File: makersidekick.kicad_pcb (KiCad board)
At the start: 2 copper layers, 50.8 x 22.9 mm, 30 parts, among them J2 Conn_01x12, J4 Conn_01x16

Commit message: Add hardware, almost finalize routing TODO: actually finish the pins
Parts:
- removed the REF** at (125.0, 75.5)
- removed kibuzzard-668B7879: G***, kibuzzard-668B7879
- removed kibuzzard-668B789B (x2): G***, kibuzzard-668B789B
- removed kibuzzard-668B795C: G***, kibuzzard-668B795C
- removed kibuzzard-668B797C: G***, kibuzzard-668B797C
- removed kibuzzard-668B7995: G***, kibuzzard-668B7995
- removed kibuzzard-668B79B7: G***, kibuzzard-668B79B7
- removed kibuzzard-668B79F7: G***, kibuzzard-668B79F7
- removed kibuzzard-668B7A0A: G***, kibuzzard-668B7A0A
- removed kibuzzard-668B7A1E: G***, kibuzzard-668B7A1E
- removed kibuzzard-668B7A2D: G***, kibuzzard-668B7A2D
- removed kibuzzard-668B7A62 (x2): G***, kibuzzard-668B7A62
- removed kibuzzard-668B7A7C: G***, kibuzzard-668B7A7C
- removed kibuzzard-668CCB83: G***, kibuzzard-668CCB83
- removed kibuzzard-668CCB9F: G***, kibuzzard-668CCB9F
- removed kibuzzard-668CCC45: G***, kibuzzard-668CCC45
- removed kibuzzard-668CCC52: G***, kibuzzard-668CCC52
- removed kibuzzard-668CCD74: G***, kibuzzard-668CCD74
- removed kibuzzard-668CCD89: G***, kibuzzard-668CCD89
- removed kibuzzard-668CCD9D: G***, kibuzzard-668CCD9D
- removed kibuzzard-668CCDA5: G***, kibuzzard-668CCDA5
- removed kibuzzard-668CCDB1: G***, kibuzzard-668CCDB1
- removed kibuzzard-668CE341: G***, kibuzzard-668CE341
- removed kibuzzard-668CE34C: G***, kibuzzard-668CE34C
- added ?: , , F.Cu at (180.3, 87.4)
- added Display 128x64 0.96" I2C: Display_128x64, TG9541:Display_128x64_096_I2C, F.Cu at (200.4, 93.0)
- added Display 128x64 0.96" I2C: Display_128x64, TG9541:Display_128x64_096_I2C, F.Cu at (197.0, 93.0)
- added REF**: module_mpu6050, usini_sensors:module_mpu6050, F.Cu at (173.0, 99.5)
- added REF**: R_Axial_DIN0204_L3.6mm_D1.6mm_P7.62mm_Horizontal, Resistor_THT:R_Axial_DIN0204_L3.6mm_D1.6mm_P7.62mm_Horizontal, F.Cu at (188.0, 85.3)
- moved REF** 1.06 mm to (182.5, 95.9)
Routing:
- net (no net): track 0.00 -> 225.3 mm
- net unconnected-(J2-Pin_8-Pad8): track 0.00 -> 9.30 mm
- net /GPIO_9: track 0.00 -> 2.07 mm
- net /SCL: track 0.75 -> 0.00 mm
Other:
- board size 50.8 x 22.9 mm -> 58.9 x 22.9 mm
- board text removed: "BOOT"
- board text removed: "RESET"

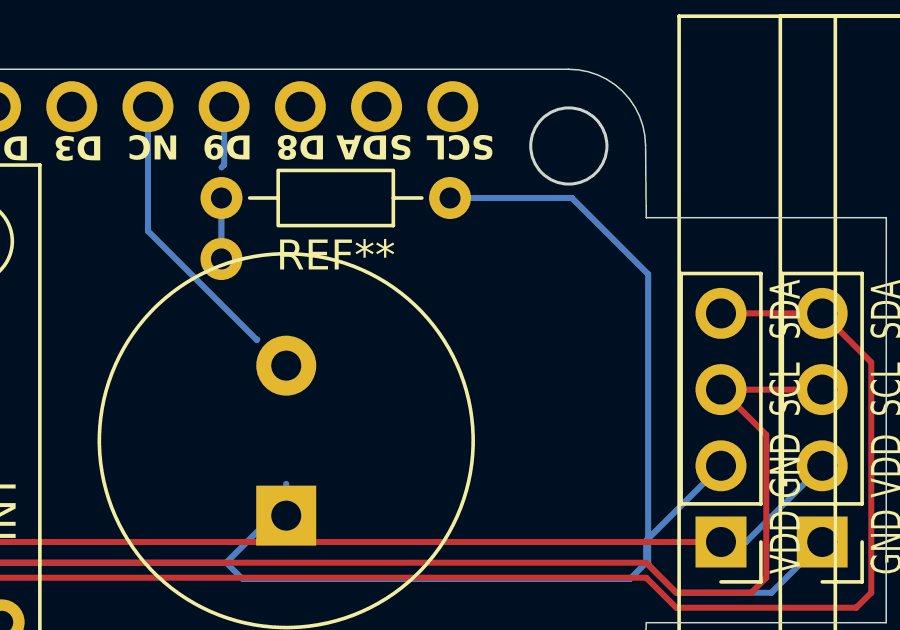
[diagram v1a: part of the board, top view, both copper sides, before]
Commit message: Add header pins to schematic(initial)
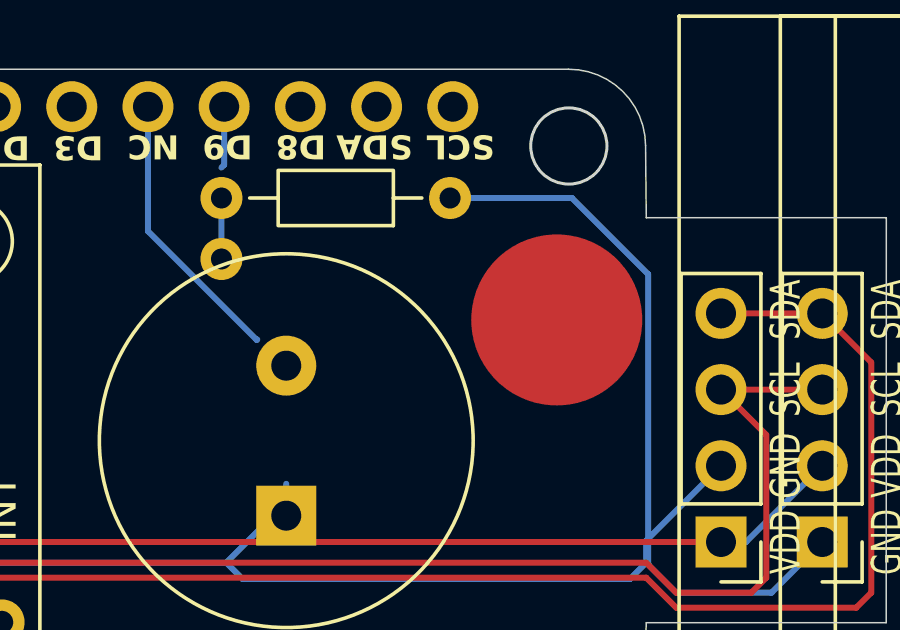
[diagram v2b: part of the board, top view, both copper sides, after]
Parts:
- added ?: , , F.Cu at (191.5, 89.4)
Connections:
- J2 pad 1: +BATT -> unconnected-(J2-Pin_1-Pad1)
- J2 pad 10: /GPIO_8 -> unconnected-(J2-Pin_10-Pad10)
- J2 pad 11: /SDA -> unconnected-(J2-Pin_11-Pad11)
- J2 pad 12: /SCL -> unconnected-(J2-Pin_12-Pad12)
- J2 pad 2: /RESET -> unconnected-(J2-Pin_2-Pad2)
- J2 pad 3: VBUS -> unconnected-(J2-Pin_3-Pad3)
- J2 pad 4: /BATT_MSR -> unconnected-(J2-Pin_4-Pad4)
- J2 pad 5: /GPIO_1 -> unconnected-(J2-Pin_5-Pad5)
- J2 pad 6: /GPIO_2 -> unconnected-(J2-Pin_6-Pad6)
- J2 pad 7: /GPIO_3 -> unconnected-(J2-Pin_7-Pad7)
- J2 pad 9: /GPIO_9 -> unconnected-(J2-Pin_9-Pad9)
- J4 pad 1: /RESET -> unconnected-(J4-Pin_1-Pad1)
- J4 pad 10: /USB_D+ -> unconnected-(J4-Pin_10-Pad10)
- J4 pad 11: /SCK -> unconnected-(J4-Pin_11-Pad11)
- J4 pad 12: /MOSI -> unconnected-(J4-Pin_12-Pad12)
- J4 pad 13: /MISO -> unconnected-(J4-Pin_13-Pad13)
- J4 pad 14: /uRx -> unconnected-(J4-Pin_14-Pad14)
- J4 pad 15: /uTx -> unconnected-(J4-Pin_15-Pad15)
- J4 pad 16: GND -> unconnected-(J4-Pin_16-Pad16)
- J4 pad 2: +3.3V -> unconnected-(J4-Pin_2-Pad2)
- J4 pad 3: +3.3V -> unconnected-(J4-Pin_3-Pad3)
- J4 pad 4: GND -> unconnected-(J4-Pin_4-Pad4)
- J4 pad 5: /BATT_MSR -> unconnected-(J4-Pin_5-Pad5)
- J4 pad 6: /GPIO_1 -> unconnected-(J4-Pin_6-Pad6)
- J4 pad 7: /GPIO_2 -> unconnected-(J4-Pin_7-Pad7)
- J4 pad 8: /GPIO_3 -> unconnected-(J4-Pin_8-Pad8)
- J4 pad 9: /USB_D- -> unconnected-(J4-Pin_9-Pad9)
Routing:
- net unconnected-(J2-Pin_9-Pad9): track 0.00 -> 2.07 mm
- net /GPIO_9: track 2.07 -> 0.00 mm
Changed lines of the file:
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@@
 	)
 	(net 0 "")
-	(net 1 "/SCL")
-	(net 2 "/RESET")
-	(net 3 "+3.3V")
-	(net 4 "GND")
-	(net 5 "/BATT_MSR")
-	(net 6 "/GPIO_1")
-	(net 7 "/GPIO_2")
-	(net 8 "/GPIO_3")
-	(net 9 "/USB_D-")
-	(net 10 "/USB_D+")
-	(net 11 "/SCK")
-	(net 12 "/MOSI")
-	(net 13 "/MISO")
-	(net 14 "/uRx")
-	(net 15 "/uTx")
-	(net 16 "+BATT")
-	(net 17 "VBUS")
-	(net 18 "unconnected-(J2-Pin_8-Pad8)")
-	(net 19 "/GPIO_9")
-	(net 20 "/GPIO_8")
-	(net 21 "/SDA")
+	(net 1 "unconnected-(J4-Pin_9-Pad9)")
+	(net 2 "unconnected-(J4-Pin_8-Pad8)")
+	(net 3 "unconnected-(J4-Pin_16-Pad16)")
+	(net 4 "unconnected-(J4-Pin_6-Pad6)")
+	(net 5 "unconnected-(J4-Pin_15-Pad15)")
+	(net 6 "unconnected-(J4-Pin_1-Pad1)")
+	(net 7 "unconnected-(J4-Pin_12-Pad12)")
+	(net 8 "unconnected-(J4-Pin_11-Pad11)")
+	(net 9 "unconnected-(J4-Pin_4-Pad4)")
+	(net 10 "unconnected-(J4-Pin_13-Pad13)")
+	(net 11 "unconnected-(J2-Pin_8-Pad8)")
+	(net 12 "unconnected-(J4-Pin_7-Pad7)")
+	(net 13 "unconnected-(J4-Pin_2-Pad2)")
+	(net 14 "unconnected-(J4-Pin_3-Pad3)")
+	(net 15 "unconnected-(J4-Pin_5-Pad5)")
+	(net 16 "unconnected-(J4-Pin_14-Pad14)")
+	(net 17 "unconnected-(J4-Pin_10-Pad10)")
+	(net 18 "unconnected-(J2-Pin_9-Pad9)")
+	(net 19 "unconnected-(J2-Pin_7-Pad7)")
+	(net 20 "unconnected-(J2-Pin_5-Pad5)")
+	(net 21 "unconnected-(J2-Pin_4-Pad4)")
+	(net 22 "unconnected-(J2-Pin_12-Pad12)")
+	(net 23 "unconnected-(J2-Pin_3-Pad3)")
+	(net 24 "unconnected-(J2-Pin_10-Pad10)")
+	(net 25 "unconnected-(J2-Pin_11-Pad11)")
+	(net 26 "unconnected-(J2-Pin_1-Pad1)")
+	(net 27 "unconnected-(J2-Pin_6-Pad6)")
+	(net 28 "unconnected-(J2-Pin_2-Pad2)")
 	(footprint "Connector_PinSocket_2.54mm:PinSocket_1x16_P2.54mm_Vertical"
 		(layer "F.Cu")
@@
 			)
 		)
+		(sheetname "/")
+		(sheetfile "makersidekick.kicad_sch")
 		(attr through_hole dnp allow_soldermask_bridges)
 		(fp_line
@@
 			(keep_end_layers yes)
 			(zone_layer_connections)
-			(net 2 "/RESET")
+			(net 6 "unconnected-(J4-Pin_1-Pad1)")
 			(pinfunction "Pin_1")
 			(pintype "passive")
@@
 			(keep_end_layers yes)
 			(zone_layer_connections)
-			(net 3 "+3.3V")
+			(net 13 "unconnected-(J4-Pin_2-Pad2)")
 			(pinfunction "Pin_2")
 			(pintype "passive")
@@
 			(keep_end_layers yes)
 			(zone_layer_connections)
-			(net 3 "+3.3V")
+			(net 14 "unconnected-(J4-Pin_3-Pad3)")
 			(pinfunction "Pin_3")
 			(pintype "passive")
@@
 			(keep_end_layers yes)
 			(zone_layer_connections)
-			(net 4 "GND")
+			(net 9 "unconnected-(J4-Pin_4-Pad4)")
 			(pinfunction "Pin_4")
 			(pintype "passive")
@@
 			(keep_end_layers yes)
 			(zone_layer_connections)
-			(net 5 "/BATT_MSR")
+			(net 15 "unconnected-(J4-Pin_5-Pad5)")
 			(pinfunction "Pin_5")
 			(pintype "passive")
@@
 			(keep_end_layers yes)
 			(zone_layer_connections)
-			(net 6 "/GPIO_1")
+			(net 4 "unconnected-(J4-Pin_6-Pad6)")
 			(pinfunction "Pin_6")
 			(pintype "passive")
@@
 			(keep_end_layers yes)
 			(zone_layer_connections)
-			(net 7 "/GPIO_2")
+			(net 12 "unconnected-(J4-Pin_7-Pad7)")
 			(pinfunction "Pin_7")
 			(pintype "passive")
@@
 			(keep_end_layers yes)
 			(zone_layer_connections)
-			(net 8 "/GPIO_3")
+			(net 2 "unconnected-(J4-Pin_8-Pad8)")
 			(pinfunction "Pin_8")
 			(pintype "passive")
@@
 			(keep_end_layers yes)
 			(zone_layer_connections)
-			(net 9 "/USB_D-")
+			(net 1 "unconnected-(J4-Pin_9-Pad9)")
 			(pinfunction "Pin_9")
 			(pintype "passive")
@@
 			(keep_end_layers yes)
 			(zone_layer_connections)
-			(net 10 "/USB_D+")
+			(net 17 "unconnected-(J4-Pin_10-Pad10)")
 			(pinfunction "Pin_10")
 			(pintype "passive")
@@
 			(keep_end_layers yes)
 			(zone_layer_connections)
-			(net 11 "/SCK")
+			(net 8 "unconnected-(J4-Pin_11-Pad11)")
 			(pinfunction "Pin_11")
 			(pintype "passive")
@@
 			(keep_end_layers yes)
 			(zone_layer_connections)
-			(net 12 "/MOSI")
+			(net 7 "unconnected-(J4-Pin_12-Pad12)")
 			(pinfunction "Pin_12")
 			(pintype "passive")
@@
 			(keep_end_layers yes)
 			(zone_layer_connections)
-			(net 13 "/MISO")
+			(net 10 "unconnected-(J4-Pin_13-Pad13)")
 			(pinfunction "Pin_13")
 			(pintype "passive")
@@
 			(keep_end_layers yes)
 			(zone_layer_connections)
-			(net 14 "/uRx")
+			(net 16 "unconnected-(J4-Pin_14-Pad14)")
 			(pinfunction "Pin_14")
 			(pintype "passive")
@@
 			(keep_end_layers yes)
 			(zone_layer_connections)
-			(net 15 "/uTx")
+			(net 5 "unconnected-(J4-Pin_15-Pad15)")
 			(pinfunction "Pin_15")
 			(pintype "passive")
@@
 			(keep_end_layers yes)
 			(zone_layer_connections)
-			(net 4 "GND")
+			(net 3 "unconnected-(J4-Pin_16-Pad16)")
 			(pinfunction "Pin_16")
 			(pintype "passive")
@@
 		(embedded_fonts no)
 	)
+	(footprint ""
+		(layer "F.Cu")
+		(at 191.516 89.408)
+		(property "Reference" ""
+			(at 0 0 0)
+			(layer "F.SilkS")
+			(effects
+				(font
+					(size 1.27 1.27)
+					(thickness 0.15)
+				)
+			)
+		)
+		(property "Value" ""
+			(at 0 0 0)
+			(layer "F.Fab")
+			(effects
+				(font
+					(size 1.27 1.27)
+					(thickness 0.15)
+				)
+			)
+		)
+		(property "Datasheet" ""
+			(at 0 0 0)
+			(layer "F.Fab")
+			(hide yes)
+			(effects
+				(font
+					(size 1.27 1.27)
+					(thickness 0.15)
+				)
+			)
+		)
+		(property "Description" ""
+			(at 0 0 0)
+			(layer "F.Fab")
+			(hide yes)
+			(effects
+				(font
+					(size 1.27 1.27)
+					(thickness 0.15)
+				)
+			)
+		)
+		(pad "3" smd circle
+			(at 0 0)
+			(size 5.7 5.7)
+			(layers "F.Cu" "F.Mask" "F.Paste")
+		)
+		(embedded_fonts no)
+	)
 	(footprint "Resistor_THT:R_Axial_DIN0204_L3.6mm_D1.6mm_P7.62mm_Horizontal"
 		(layer "F.Cu")
@@
 			(at 3.81 -1.92 0)
 			(layer "F.SilkS")
+			(hide yes)
 			(effects
 				(font
@@
 			)
 		)
+		(sheetname "/")
+		(sheetfile "makersidekick.kicad_sch")
 		(attr through_hole dnp)
 		(fp_line
@@
 			(layers "*.Cu" "*.Mask")
 			(remove_unused_layers no)
-			(net 16 "+BATT")
+			(net 26 "unconnected-(J2-Pin_1-Pad1)")
 			(pinfunction "Pin_1")
 			(pintype "passive")
@@
 			(layers "*.Cu" "*.Mask")
 			(remove_unused_layers no)
-			(net 2 "/RESET")
+			(net 28 "unconnected-(J2-Pin_2-Pad2)")
 			(pinfunction "Pin_2")
 			(pintype "passive")
@@
 			(layers "*.Cu" "*.Mask")
 			(remove_unused_layers no)
-			(net 17 "VBUS")
+			(net 23 "unconnected-(J2-Pin_3-Pad3)")
 			(pinfunction "Pin_3")
 			(pintype "passive")
@@
 			(layers "*.Cu" "*.Mask")
 			(remove_unused_layers no)
-			(net 5 "/BATT_MSR")
+			(net 21 "unconnected-(J2-Pin_4-Pad4)")
 			(pinfunction "Pin_4")
 			(pintype "passive")
@@
 			(layers "*.Cu" "*.Mask")
 			(remove_unused_layers no)
-			(net 6 "/GPIO_1")
+			(net 20 "unconnected-(J2-Pin_5-Pad5)")
 			(pinfunction "Pin_5")
 			(pintype "passive")
@@
 			(layers "*.Cu" "*.Mask")
 			(remove_unused_layers no)
-			(net 7 "/GPIO_2")
+			(net 27 "unconnected-(J2-Pin_6-Pad6)")
 			(pinfunction "Pin_6")
 			(pintype "passive")
@@
 			(layers "*.Cu" "*.Mask")
 			(remove_unused_layers no)
-			(net 8 "/GPIO_3")
+			(net 19 "unconnected-(J2-Pin_7-Pad7)")
 			(pinfunction "Pin_7")
 			(pintype "passive")
@@
 			(layers "*.Cu" "*.Mask")
 			(remove_unused_layers no)
-			(net 18 "unconnected-(J2-Pin_8-Pad8)")
+			(net 11 "unconnected-(J2-Pin_8-Pad8)")
 			(pinfunction "Pin_8")
-			(pintype "passive+no_connect")
+			(pintype "passive")
 			(teardrops
 				(best_length_ratio 0.5)
@@
 			(layers "*.Cu" "*.Mask")
 			(remove_unused_layers no)
-			(net 19 "/GPIO_9")
+			(net 18 "unconnected-(J2-Pin_9-Pad9)")
 			(pinfunction "Pin_9")
 			(pintype "passive")
@@
 			(layers "*.Cu" "*.Mask")
 			(remove_unused_layers no)
-			(net 20 "/GPIO_8")
+			(net 24 "unconnected-(J2-Pin_10-Pad10)")
 			(pinfunction "Pin_10")
 			(pintype "passive")
@@
 			(layers "*.Cu" "*.Mask")
 			(remove_unused_layers no)
-			(net 21 "/SDA")
+			(net 25 "unconnected-(J2-Pin_11-Pad11)")
 			(pinfunction "Pin_11")
 			(pintype "passive")
@@
 			(layers "*.Cu" "*.Mask")
 			(remove_unused_layers no)
-			(net 1 "/SCL")
+			(net 22 "unconnected-(J2-Pin_12-Pad12)")
 			(pinfunction "Pin_12")
 			(pintype "passive")
@@
 		(width 0.2)
 		(layer "B.Cu")
-		(net 18)
+		(net 11)
 	)
 	(segment
@@
 		(width 0.2)
 		(layer "B.Cu")
-		(net 18)
+		(net 11)
 	)
 	(segment
@@
 		(width 0.2)
 		(layer "B.Cu")
-		(net 18)
+		(net 11)
 	)
 	(segment
@@
 		(width 0.2)
 		(layer "B.Cu")
-		(net 19)
+		(net 18)
 	)
 	(segment
@@
 		(width 0.2)
 		(layer "B.Cu")
-		(net 19)
+		(net 18)
 	)
 	(zone
 		(net 18)
-		(net_name "unconnected-(J2-Pin_8-Pad8)")
+		(net_name "unconnected-(J2-Pin_9-Pad9)")
 		(layer "B.Cu")
 		(name "$teardrop_padvia$")
 		(hatch none 0.1)
-		(priority 30000)
+		(priority 30001)
 		(attr
 			(teardrop
@@
 		(polygon
 			(pts
-				(xy 177.79 83.983667) (xy 177.99 83.983667) (xy 178.596749 82.772235) (xy 177.89 82.299) (xy 177.183251 82.772235)
+				(xy 180.33 83.983667) (xy 180.53 83.983667) (xy 181.136749 82.772235) (xy 180.43 82.299) (xy 179.723251 82.772235)
 			)
 		)
 	)
 	(zone
-		(net 19)
-		(net_name "/GPIO_9")
+		(net 11)
+		(net_name "unconnected-(J2-Pin_8-Pad8)")
 		(layer "B.Cu")
 		(name "$teardrop_padvia$")
@@
 		(polygon
 			(pts
-				(xy 180.33 83.983667) (xy 180.53 83.983667) (xy 181.136749 82.772235) (xy 180.43 82.299) (xy 179.723251 82.772235)
+				(xy 177.79 83.983667) (xy 177.99 83.983667) (xy 178.596749 82.772235) (xy 177.89 82.299) (xy 177.183251 82.772235)
 			)
 		)

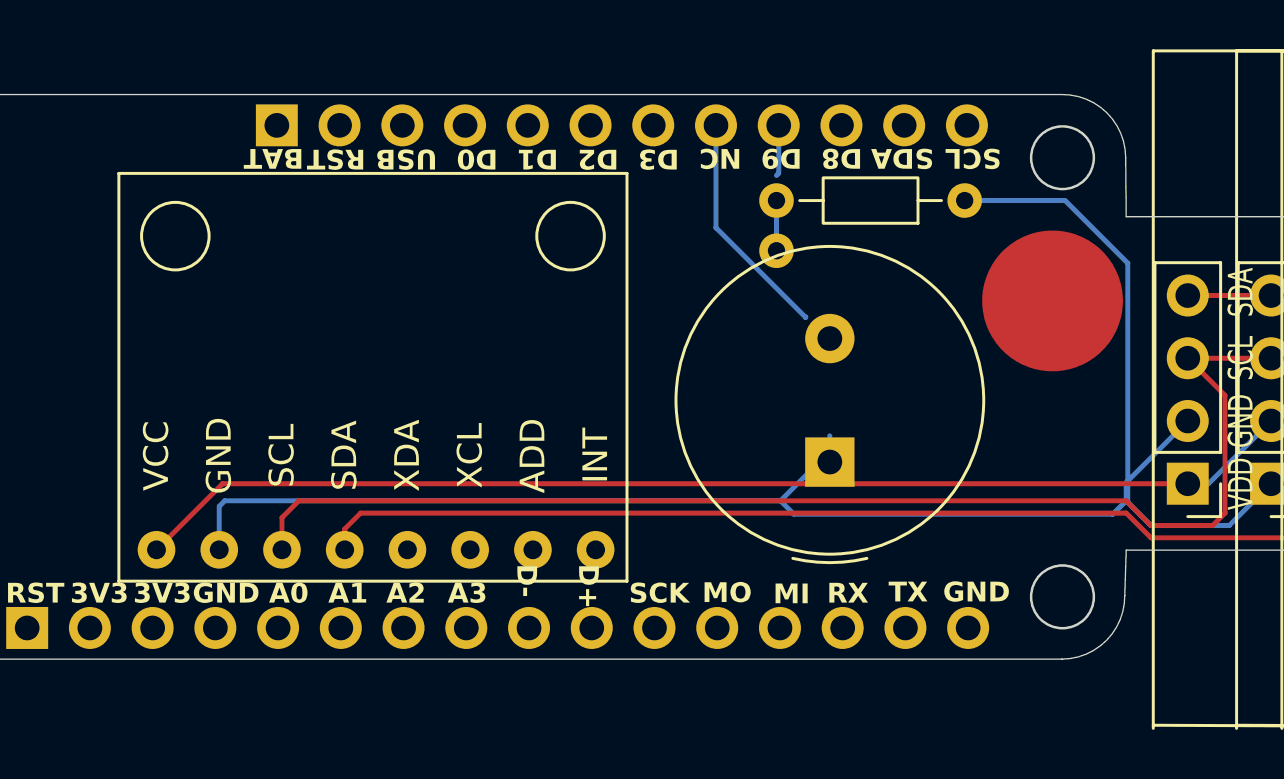
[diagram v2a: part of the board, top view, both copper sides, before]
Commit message: Assign nets, finish connection, prep for v0
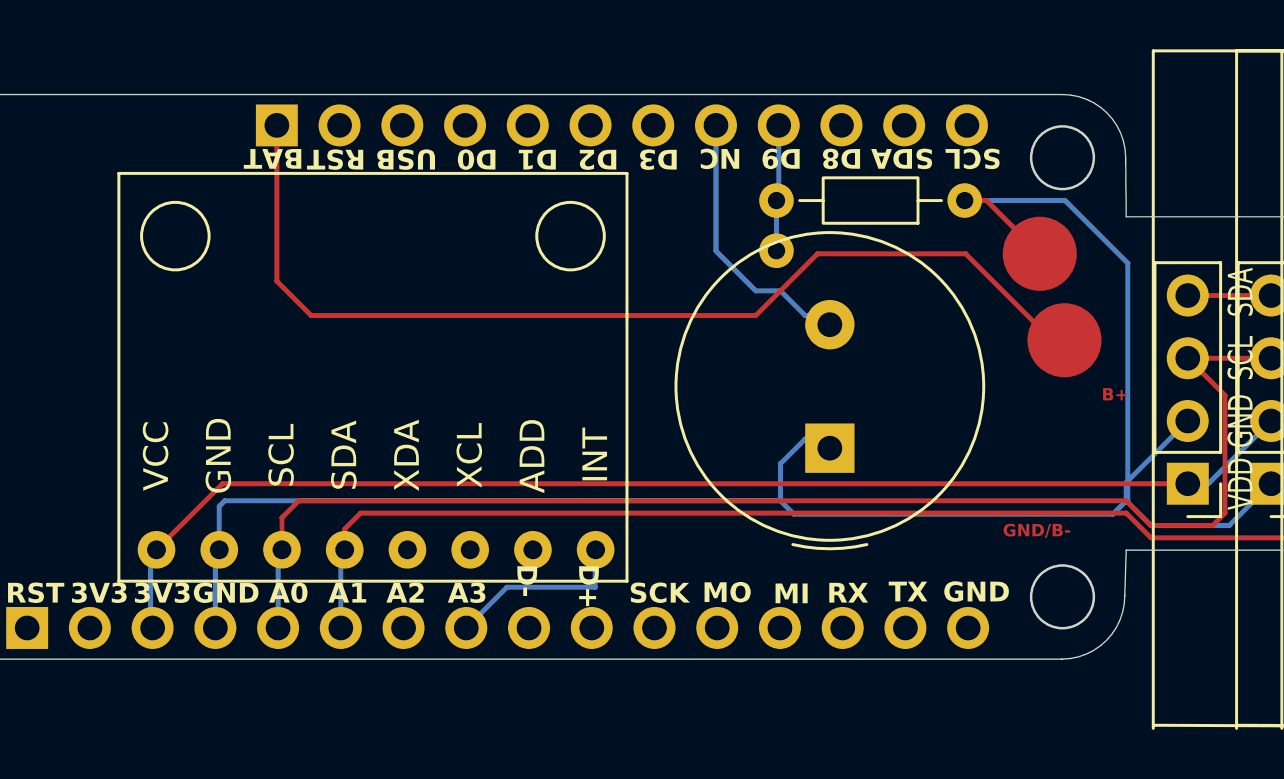
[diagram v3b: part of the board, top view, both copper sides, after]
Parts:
- added ?: , , F.Cu at (191.0, 87.5)
- moved ? 1.66 mm to (192.0, 91.0)
- moved REF** 0.56 mm to (182.5, 95.4)
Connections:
- ? pad 2: (no net) -> D9
- J2 pad 1: unconnected-(J2-Pin_1-Pad1) -> B+
- J2 pad 8: unconnected-(J2-Pin_8-Pad8) -> D8
- J2 pad 9: unconnected-(J2-Pin_9-Pad9) -> D9
- J4 pad 3: unconnected-(J4-Pin_3-Pad3) -> 3v3
- J4 pad 4: unconnected-(J4-Pin_4-Pad4) -> gnd
- J4 pad 5: unconnected-(J4-Pin_5-Pad5) -> A0
- J4 pad 6: unconnected-(J4-Pin_6-Pad6) -> A1
- J4 pad 8: unconnected-(J4-Pin_8-Pad8) -> A3
- REF** pad 1: (no net) -> gnd (x2)
- REF** pad 2: (no net) -> D8
- REF** pad 1: (no net) -> 3v3
- REF** pad 2: (no net) -> gnd
- REF** pad 3: (no net) -> A0
- REF** pad 4: (no net) -> A1
- REF** pad 8: (no net) -> A3
- REF** pad 2: (no net) -> D9
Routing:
- net (no net): track 225.3 -> 0.00 mm
- net gnd: track 0.00 -> 78.8 mm
- net A1: track 0.00 -> 57.5 mm
- net A0: track 0.00 -> 53.9 mm
- net 3v3: track 0.00 -> 50.6 mm
- net B+: track 0.00 -> 41.8 mm
- net D8: track 0.00 -> 11.3 mm
- net unconnected-(J2-Pin_8-Pad8): track 9.30 -> 0.00 mm
- net A3: track 0.00 -> 7.43 mm
- net D9: track 0.00 -> 5.11 mm
- net unconnected-(J2-Pin_9-Pad9): track 2.07 -> 0.00 mm
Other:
- board text added: "GND/B-"
